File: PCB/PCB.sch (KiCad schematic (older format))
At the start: 40 parts, among them J1 Dynamo, J10 Conn_01x08_Female, J11 Conn_01x01_Female, J12 Conn_01x04_Female, J2 Conn_01x28_Female, J3 Conn_01x02_Female, J4 Conn_01x02_Female, J5 Conn_01x02_Female, J6 Conn_01x02_Female, J7 Conn_01x08_Female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

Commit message: Added PCB images
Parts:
- removed J1: Dynamo, TerminalBlock:TerminalBlock_Altech_AK300-2_P5.00mm, symbol Connector:Screw_Terminal_01x02
- added J1: Conn_01x04_Female, Connector_Molex:Molex_KK-396_A-41791-0004_1x04_P3.96mm_Vertical, symbol Connector:Conn_01x04_Female
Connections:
- net at D2.1 (K), D4.2 (A): now also J1.1 (Pin_1), J1.2 (Pin_2)
- net at D1.1 (K), D3.2 (A): now also J1.3 (Pin_3), J1.4 (Pin_4)
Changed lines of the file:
@@
 EESchema Schematic File Version 4
 LIBS:PCB-cache
-EELAYER 29 0
+EELAYER 26 0
 EELAYER END
 $Descr A4 11693 8268
@@
 	-1   0    0    1
 $EndComp
-$Comp
-L Connector:Screw_Terminal_01x02 J1
-U 1 1 5E63414E
-P 1550 1300
-F 0 "J1" H 1550 950 50  0000 C CNN
-F 1 "Dynamo" H 1550 1050 50  0000 C CNN
-F 2 "TerminalBlock:TerminalBlock_Altech_AK300-2_P5.00mm" H 1550 1300 50  0001 C CNN
-F 3 "~" H 1550 1300 50  0001 C CNN
-	1    1550 1300
-	-1   0    0    1
-$EndComp
 Wire Wire Line
 	2100 1050 2000 1050
@@
 NoConn ~ 2850 4450
 NoConn ~ 2850 4550
+$Comp
+L Connector:Conn_01x04_Female J1
+U 1 1 5E2F9CB0
+P 1450 1300
+F 0 "J1" H 1344 875 50  0000 C CNN
+F 1 "Conn_01x04_Female" H 1344 966 50  0000 C CNN
+F 2 "Connector_Molex:Molex_KK-396_A-41791-0004_1x04_P3.96mm_Vertical" H 1450 1300 50  0001 C CNN
+F 3 "~" H 1450 1300 50  0001 C CNN
+	1    1450 1300
+	-1   0    0    1
+$EndComp
+Wire Wire Line
+	1750 1200 1650 1200
+Wire Wire Line
+	1750 1300 1650 1300
+Wire Wire Line
+	1650 1200 1650 1100
+Connection ~ 1650 1200
+Wire Wire Line
+	1650 1300 1650 1400
+Connection ~ 1650 1300
 $EndSCHEMATC

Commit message: Added GPS control logic
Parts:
- added Q1: PN2222A, Package_TO_SOT_THT:TO-92_Inline, symbol Transistor_BJT:PN2222A
- added Q2: IRF4905, Package_TO_SOT_THT:TO-220-3_Vertical, symbol Transistor_FET:IRF4905
- added R3: 1k, Resistor_THT:R_Axial_DIN0207_L6.3mm_D2.5mm_P10.16mm_Horizontal, symbol Device:R
- added R4: 4.7k, Resistor_THT:R_Axial_DIN0207_L6.3mm_D2.5mm_P10.16mm_Horizontal, symbol Device:R
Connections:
- net +5V: now also Q2.3 (S), R4.2; no longer J12.1 (Pin_1)
- net GND: now also Q1.1 (E)
- net GPSEN: now reaches J2.28 (Pin_28)
- net GPSEN: now also R3.1
- new net: Q1.2 (B), R3.2
- new net: Q1.3 (C), Q2.1 (G), R4.1
- new net VCCGPS: J12.1 (Pin_1), Q2.2 (D)
- no-connect marks 14 -> 13
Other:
- moved on the sheet: C15, J12, J8, R2
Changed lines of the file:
@@
 $EndComp
 Wire Wire Line
-	9650 5300 9500 5300
-Wire Wire Line
-	9650 5400 9500 5400
-Text GLabel 9500 5400 0    50   Input ~ 0
+	9100 4200 8950 4200
+Wire Wire Line
+	9100 4300 8950 4300
+Text GLabel 8950 4300 0    50   Input ~ 0
 RX
 Wire Wire Line
@@
 Text GLabel 2650 5650 0    50   Input ~ 0
 RX
-Text GLabel 9500 5300 0    50   Input ~ 0
+Text GLabel 8950 4200 0    50   Input ~ 0
 TX
 Wire Wire Line
@@
 TX
 Wire Wire Line
-	9650 5500 9500 5500
-Wire Wire Line
-	9650 5200 9500 5200
-Wire Wire Line
-	9500 5200 9500 5150
-$Comp
-L power:+5V #PWR026
-U 1 1 5E2D514F
-P 9500 5150
-F 0 "#PWR026" H 9500 5000 50  0001 C CNN
-F 1 "+5V" H 9515 5323 50  0000 C CNN
-F 2 "" H 9500 5150 50  0001 C CNN
-F 3 "" H 9500 5150 50  0001 C CNN
-	1    9500 5150
-	1    0    0    -1
-$EndComp
-Wire Wire Line
-	9500 5500 9500 5550
+	9100 4400 8950 4400
+Wire Wire Line
+	9100 4100 8950 4100
+Wire Wire Line
+	8950 4400 8950 4450
 $Comp
 L power:GND #PWR027
 U 1 1 5E2D7839
-P 9500 5550
-F 0 "#PWR027" H 9500 5300 50  0001 C CNN
-F 1 "GND" H 9505 5377 50  0000 C CNN
-F 2 "" H 9500 5550 50  0001 C CNN
-F 3 "" H 9500 5550 50  0001 C CNN
-	1    9500 5550
+P 8950 4450
+F 0 "#PWR027" H 8950 4200 50  0001 C CNN
+F 1 "GND" H 8955 4277 50  0000 C CNN
+F 2 "" H 8950 4450 50  0001 C CNN
+F 3 "" H 8950 4450 50  0001 C CNN
+	1    8950 4450
 	1    0    0    -1
 $EndComp
@@
 	6450 1650 6850 1650
 Wire Wire Line
-	8650 5350 8650 5650
+	7900 4250 7900 4550
 $Comp
 L power:GND #PWR021
 U 1 1 5E671D81
-P 8650 5650
-F 0 "#PWR021" H 8650 5400 50  0001 C CNN
-F 1 "GND" H 8655 5477 50  0000 C CNN
-F 2 "" H 8650 5650 50  0001 C CNN
-F 3 "" H 8650 5650 50  0001 C CNN
-	1    8650 5650
+P 7900 4550
+F 0 "#PWR021" H 7900 4300 50  0001 C CNN
+F 1 "GND" H 7905 4377 50  0000 C CNN
+F 2 "" H 7900 4550 50  0001 C CNN
+F 3 "" H 7900 4550 50  0001 C CNN
+	1    7900 4550
 	1    0    0    -1
 $EndComp
@@
 L Connector:Conn_01x04_Female J12
 U 1 1 5E3CD64F
-P 9850 5300
-F 0 "J12" H 9878 5276 50  0000 L CNN
-F 1 "Conn_01x04_Female" H 9878 5185 50  0000 L CNN
-F 2 "Connector_PinSocket_2.54mm:PinSocket_1x04_P2.54mm_Vertical" H 9850 5300 50  0001 C CNN
-F 3 "~" H 9850 5300 50  0001 C CNN
-	1    9850 5300
+P 9300 4200
+F 0 "J12" H 9328 4176 50  0000 L CNN
+F 1 "Conn_01x04_Female" H 9328 4085 50  0000 L CNN
+F 2 "Connector_PinSocket_2.54mm:PinSocket_1x04_P2.54mm_Vertical" H 9300 4200 50  0001 C CNN
+F 3 "~" H 9300 4200 50  0001 C CNN
+	1    9300 4200
 	1    0    0    -1
 $EndComp
@@
 L Connector:Conn_01x02_Female J8
 U 1 1 5E3EA4DC
-P 8300 5150
-F 0 "J8" V 8238 4962 50  0000 R CNN
-F 1 "Conn_01x02_Female" V 8147 4962 50  0000 R CNN
-F 2 "Connector_Molex:Molex_PicoBlade_53047-0210_1x02_P1.25mm_Vertical" H 8300 5150 50  0001 C CNN
-F 3 "~" H 8300 5150 50  0001 C CNN
-	1    8300 5150
+P 7550 4050
+F 0 "J8" V 7488 3862 50  0000 R CNN
+F 1 "Conn_01x02_Female" V 7397 3862 50  0000 R CNN
+F 2 "Connector_Molex:Molex_PicoBlade_53047-0210_1x02_P1.25mm_Vertical" H 7550 4050 50  0001 C CNN
+F 3 "~" H 7550 4050 50  0001 C CNN
+	1    7550 4050
 	0    -1   -1   0
 $EndComp
 Wire Wire Line
-	8400 5350 8650 5350
+	7650 4250 7900 4250
 $Comp
 L Connector:Conn_01x08_Female J7
@@
 NSS
 $Comp
-L Connector:Conn_01x28_Female J2
-U 1 1 5E7FA35C
-P 3050 5650
-F 0 "J2" H 3078 5626 50  0000 L CNN
-F 1 "Conn_01x28_Female" H 3078 5535 50  0000 L CNN
-F 2 "Package_DIP:DIP-28_W7.62mm" H 3050 5650 50  0001 C CNN
-F 3 "~" H 3050 5650 50  0001 C CNN
-	1    3050 5650
-	1    0    0    -1
-$EndComp
-$Comp
 L Device:C_Small C5
 U 1 1 5E7AF997
@@
 NoConn ~ 2850 6850
 NoConn ~ 2850 6950
-NoConn ~ 2850 7050
 $Comp
 L Connector:Conn_01x02_Female J3
@@
 	8500 1250 8900 1250
 NoConn ~ 2850 6650
-Text GLabel 7600 5350 0    50   Input ~ 0
+Text GLabel 6850 4250 0    50   Input ~ 0
 BUTTON
 $Comp
 L Device:R R2
 U 1 1 5ECC6F67
-P 7900 5350
-F 0 "R2" V 8050 5350 50  0000 L CNN
-F 1 "1k" V 7970 5305 50  0000 L CNN
-F 2 "Resistor_THT:R_Axial_DIN0207_L6.3mm_D2.5mm_P10.16mm_Horizontal" V 7830 5350 50  0001 C CNN
-F 3 "~" H 7900 5350 50  0001 C CNN
-	1    7900 5350
+P 7150 4250
+F 0 "R2" V 7300 4250 50  0000 L CNN
+F 1 "1k" V 7220 4205 50  0000 L CNN
+F 2 "Resistor_THT:R_Axial_DIN0207_L6.3mm_D2.5mm_P10.16mm_Horizontal" V 7080 4250 50  0001 C CNN
+F 3 "~" H 7150 4250 50  0001 C CNN
+	1    7150 4250
 	0    -1   -1   0
 $EndComp
 Wire Wire Line
-	7600 5350 7750 5350
-Wire Wire Line
-	8200 5350 8300 5350
-Connection ~ 8200 5350
-Wire Wire Line
-	8050 5350 8200 5350
+	6850 4250 7000 4250
+Wire Wire Line
+	7450 4250 7550 4250
+Connection ~ 7450 4250
+Wire Wire Line
+	7300 4250 7450 4250
 $Comp
 L power:GND #PWR018
 U 1 1 5ECB146B
-P 8200 5650
-F 0 "#PWR018" H 8200 5400 50  0001 C CNN
-F 1 "GND" H 8205 5477 50  0000 C CNN
-F 2 "" H 8200 5650 50  0001 C CNN
-F 3 "" H 8200 5650 50  0001 C CNN
-	1    8200 5650
-	1    0    0    -1
-$EndComp
-Wire Wire Line
-	8200 5350 8200 5400
-Wire Wire Line
-	8200 5600 8200 5650
+P 7450 4550
+F 0 "#PWR018" H 7450 4300 50  0001 C CNN
+F 1 "GND" H 7455 4377 50  0000 C CNN
+F 2 "" H 7450 4550 50  0001 C CNN
+F 3 "" H 7450 4550 50  0001 C CNN
+	1    7450 4550
+	1    0    0    -1
+$EndComp
+Wire Wire Line
+	7450 4250 7450 4300
+Wire Wire Line
+	7450 4500 7450 4550
 $Comp
 L Device:C_Small C15
 U 1 1 5EC75BB7
-P 8200 5500
-F 0 "C15" H 8292 5546 50  0000 L CNN
-F 1 "100n" H 8292 5455 50  0000 L CNN
-F 2 "Capacitor_THT:C_Disc_D3.0mm_W2.0mm_P2.50mm" H 8200 5500 50  0001 C CNN
-F 3 "~" H 8200 5500 50  0001 C CNN
-	1    8200 5500
+P 7450 4400
+F 0 "C15" H 7542 4446 50  0000 L CNN
+F 1 "100n" H 7542 4355 50  0000 L CNN
+F 2 "Capacitor_THT:C_Disc_D3.0mm_W2.0mm_P2.50mm" H 7450 4400 50  0001 C CNN
+F 3 "~" H 7450 4400 50  0001 C CNN
+	1    7450 4400
 	1    0    0    -1
 $EndComp
@@
 	1650 1300 1650 1400
 Connection ~ 1650 1300
+$Comp
+L Device:R R3
+U 1 1 5E30BB98
+P 7250 5850
+F 0 "R3" V 7457 5850 50  0000 C CNN
+F 1 "1k" V 7366 5850 50  0000 C CNN
+F 2 "Resistor_THT:R_Axial_DIN0207_L6.3mm_D2.5mm_P10.16mm_Horizontal" V 7180 5850 50  0001 C CNN
+F 3 "~" H 7250 5850 50  0001 C CNN
+	1    7250 5850
+	0    -1   -1   0
+$EndComp
+$Comp
+L Device:R R4
+U 1 1 5E31ACDB
+P 7400 5400
+F 0 "R4" H 7330 5354 50  0000 R CNN
+F 1 "4.7k" H 7330 5445 50  0000 R CNN
+F 2 "Resistor_THT:R_Axial_DIN0207_L6.3mm_D2.5mm_P10.16mm_Horizontal" V 7330 5400 50  0001 C CNN
+F 3 "~" H 7400 5400 50  0001 C CNN
+	1    7400 5400
+	-1   0    0    1
+$EndComp
+$Comp
+L Transistor_BJT:PN2222A Q1
+U 1 1 5E338DF7
+P 7750 5850
+F 0 "Q1" H 7941 5896 50  0000 L CNN
+F 1 "PN2222A" H 7941 5805 50  0000 L CNN
+F 2 "Package_TO_SOT_THT:TO-92_Inline" H 7950 5775 50  0001 L CIN
+F 3 "http://www.fairchildsemi.com/ds/PN/PN2222A.pdf" H 7750 5850 50  0001 L CNN
+	1    7750 5850
+	1    0    0    -1
+$EndComp
+$Comp
+L Transistor_FET:IRF4905 Q2
+U 1 1 5E338EAB
+P 7850 5300
+F 0 "Q2" V 8193 5300 50  0000 C CNN
+F 1 "IRF4905" V 8102 5300 50  0000 C CNN
+F 2 "Package_TO_SOT_THT:TO-220-3_Vertical" H 8050 5225 50  0001 L CIN
+F 3 "http://www.infineon.com/dgdl/irf4905.pdf?fileId=5546d462533600a4015355e32165197c" H 7850 5300 50  0001 L CNN
+	1    7850 5300
+	0    1    -1   0
+$EndComp
+$Comp
+L Connector:Conn_01x28_Female J2
+U 1 1 5E7FA35C
+P 3050 5650
+F 0 "J2" H 3078 5626 50  0000 L CNN
+F 1 "Conn_01x28_Female" H 3078 5535 50  0000 L CNN
+F 2 "Package_DIP:DIP-28_W7.62mm" H 3050 5650 50  0001 C CNN
+F 3 "~" H 3050 5650 50  0001 C CNN
+	1    3050 5650
+	1    0    0    -1
+$EndComp
+Wire Wire Line
+	2850 7050 2650 7050
+Text GLabel 2650 7050 0    50   Input ~ 0
+GPSEN
+Wire Wire Line
+	7100 5850 6900 5850
+Text GLabel 6900 5850 0    50   Input ~ 0
+GPSEN
+Wire Wire Line
+	7400 5850 7550 5850
+Wire Wire Line
+	7850 6050 7850 6150
+$Comp
+L power:GND #PWR028
+U 1 1 5E397848
+P 7850 6150
+F 0 "#PWR028" H 7850 5900 50  0001 C CNN
+F 1 "GND" H 7855 5977 50  0000 C CNN
+F 2 "" H 7850 6150 50  0001 C CNN
+F 3 "" H 7850 6150 50  0001 C CNN
+	1    7850 6150
+	1    0    0    -1
+$EndComp
+Wire Wire Line
+	7850 5650 7850 5600
+Wire Wire Line
+	7850 5600 7400 5600
+Wire Wire Line
+	7400 5600 7400 5550
+Connection ~ 7850 5600
+Wire Wire Line
+	7850 5600 7850 5500
+Wire Wire Line
+	7400 5250 7400 5200
+Wire Wire Line
+	7400 5200 7650 5200
+Wire Wire Line
+	7400 5200 7400 5150
+Connection ~ 7400 5200
+$Comp
+L power:+5V #PWR026
+U 1 1 5E3C04A1
+P 7400 5150
+F 0 "#PWR026" H 7400 5000 50  0001 C CNN
+F 1 "+5V" H 7415 5323 50  0000 C CNN
+F 2 "" H 7400 5150 50  0001 C CNN
+F 3 "" H 7400 5150 50  0001 C CNN
+	1    7400 5150
+	1    0    0    -1
+$EndComp
+Wire Wire Line
+	8050 5200 8250 5200
+Text GLabel 8250 5200 2    50   Input ~ 0
+VCCGPS
+Text GLabel 8950 4100 0    50   Input ~ 0
+VCCGPS
 $EndSCHEMATC

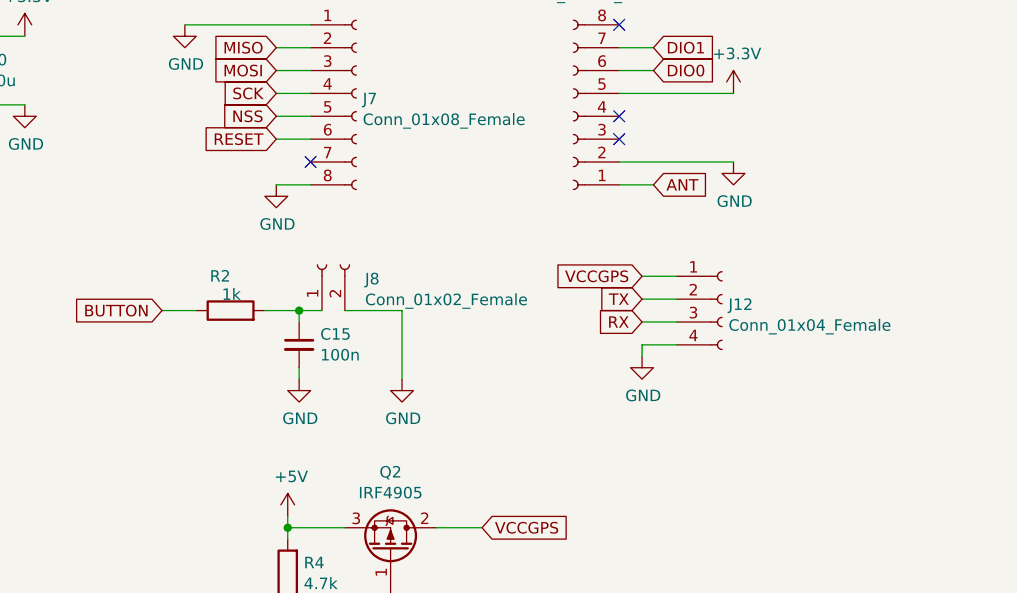
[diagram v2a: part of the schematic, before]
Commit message: fixed PCB layout and transmitter data fetch bug
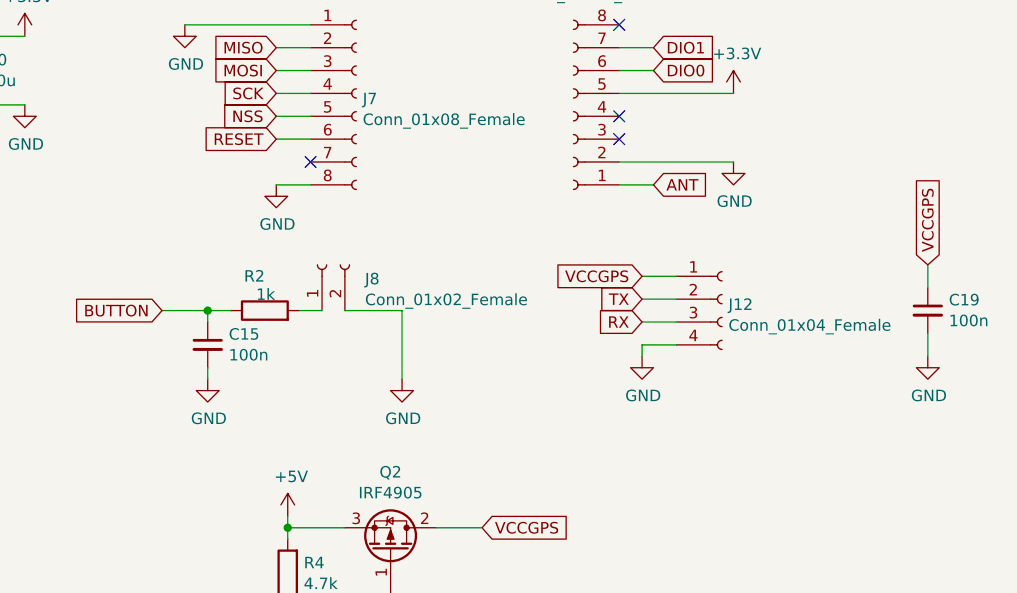
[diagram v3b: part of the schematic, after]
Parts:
- added C19: 100n, Capacitor_THT:C_Disc_D3.0mm_W2.0mm_P2.50mm, symbol Device:C_Small
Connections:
- net BUTTON: now also C15.1
- net GND: now also C19.2
- net VCCGPS: now also C19.1
- net at J8.1 (Pin_1), R2.2: no longer C15.1
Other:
- moved on the sheet: C15, R2
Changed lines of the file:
@@
 L Device:R R2
 U 1 1 5ECC6F67
-P 7150 4250
-F 0 "R2" V 7300 4250 50  0000 L CNN
-F 1 "1k" V 7220 4205 50  0000 L CNN
-F 2 "Resistor_THT:R_Axial_DIN0207_L6.3mm_D2.5mm_P10.16mm_Horizontal" V 7080 4250 50  0001 C CNN
-F 3 "~" H 7150 4250 50  0001 C CNN
-	1    7150 4250
+P 7300 4250
+F 0 "R2" V 7450 4250 50  0000 L CNN
+F 1 "1k" V 7370 4205 50  0000 L CNN
+F 2 "Resistor_THT:R_Axial_DIN0207_L6.3mm_D2.5mm_P10.16mm_Horizontal" V 7230 4250 50  0001 C CNN
+F 3 "~" H 7300 4250 50  0001 C CNN
+	1    7300 4250
 	0    -1   -1   0
 $EndComp
-Wire Wire Line
-	6850 4250 7000 4250
-Wire Wire Line
-	7450 4250 7550 4250
-Connection ~ 7450 4250
-Wire Wire Line
-	7300 4250 7450 4250
 $Comp
 L power:GND #PWR018
 U 1 1 5ECB146B
-P 7450 4550
-F 0 "#PWR018" H 7450 4300 50  0001 C CNN
-F 1 "GND" H 7455 4377 50  0000 C CNN
-F 2 "" H 7450 4550 50  0001 C CNN
-F 3 "" H 7450 4550 50  0001 C CNN
-	1    7450 4550
-	1    0    0    -1
-$EndComp
-Wire Wire Line
-	7450 4250 7450 4300
-Wire Wire Line
-	7450 4500 7450 4550
+P 7050 4550
+F 0 "#PWR018" H 7050 4300 50  0001 C CNN
+F 1 "GND" H 7055 4377 50  0000 C CNN
+F 2 "" H 7050 4550 50  0001 C CNN
+F 3 "" H 7050 4550 50  0001 C CNN
+	1    7050 4550
+	1    0    0    -1
+$EndComp
+Wire Wire Line
+	7050 4250 7050 4300
+Wire Wire Line
+	7050 4500 7050 4550
 $Comp
 L Device:C_Small C15
 U 1 1 5EC75BB7
-P 7450 4400
-F 0 "C15" H 7542 4446 50  0000 L CNN
-F 1 "100n" H 7542 4355 50  0000 L CNN
-F 2 "Capacitor_THT:C_Disc_D3.0mm_W2.0mm_P2.50mm" H 7450 4400 50  0001 C CNN
-F 3 "~" H 7450 4400 50  0001 C CNN
-	1    7450 4400
+P 7050 4400
+F 0 "C15" H 7142 4446 50  0000 L CNN
+F 1 "100n" H 7142 4355 50  0000 L CNN
+F 2 "Capacitor_THT:C_Disc_D3.0mm_W2.0mm_P2.50mm" H 7050 4400 50  0001 C CNN
+F 3 "~" H 7050 4400 50  0001 C CNN
+	1    7050 4400
 	1    0    0    -1
 $EndComp
@@
 Text GLabel 8950 4100 0    50   Input ~ 0
 VCCGPS
+Wire Wire Line
+	7450 4250 7550 4250
+Connection ~ 7050 4250
+Wire Wire Line
+	7050 4250 7150 4250
+Wire Wire Line
+	6850 4250 7050 4250
+$Comp
+L Device:C_Small C19
+U 1 1 5E40C6E0
+P 10200 4250
+F 0 "C19" H 10292 4296 50  0000 L CNN
+F 1 "100n" H 10292 4205 50  0000 L CNN
+F 2 "Capacitor_THT:C_Disc_D3.0mm_W2.0mm_P2.50mm" H 10200 4250 50  0001 C CNN
+F 3 "~" H 10200 4250 50  0001 C CNN
+	1    10200 4250
+	1    0    0    -1
+$EndComp
+Wire Wire Line
+	10200 4150 10200 4050
+Text GLabel 10200 4050 1    50   Input ~ 0
+VCCGPS
+$Comp
+L power:GND #PWR029
+U 1 1 5E436C44
+P 10200 4450
+F 0 "#PWR029" H 10200 4200 50  0001 C CNN
+F 1 "GND" H 10205 4277 50  0000 C CNN
+F 2 "" H 10200 4450 50  0001 C CNN
+F 3 "" H 10200 4450 50  0001 C CNN
+	1    10200 4450
+	1    0    0    -1
+$EndComp
+Wire Wire Line
+	10200 4350 10200 4450
 $EndSCHEMATC

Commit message: Finished Transmitter code and PCB
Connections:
- net BUTTON: now also J2.5 (Pin_5); no longer J2.23 (Pin_23)
- net DIO1: no longer J2.5 (Pin_5)
- net at J1.1 (Pin_1), J1.2 (Pin_2): now also D1.1 (K), D3.2 (A); no longer D2.1 (K), D4.2 (A)
- net at J1.3 (Pin_3), J1.4 (Pin_4): now also D2.1 (K), D4.2 (A); no longer D1.1 (K), D3.2 (A)
- no-connect marks 13 -> 14
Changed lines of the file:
@@
 DIO0
-Wire Wire Line
-	2850 4750 2650 4750
-Text GLabel 2650 4750 0    50   Input ~ 0
-DIO1
 Wire Wire Line
 	1500 4100 1700 4100
@@
 NoConn ~ 2850 5450
 NoConn ~ 2850 5550
-Text GLabel 2650 6550 0    50   Input ~ 0
-BUTTON
-Wire Wire Line
-	2850 6550 2650 6550
 Wire Wire Line
 	2850 6450 2250 6450
@@
 L Connector:Conn_01x04_Female J1
 U 1 1 5E2F9CB0
-P 1450 1300
-F 0 "J1" H 1344 875 50  0000 C CNN
-F 1 "Conn_01x04_Female" H 1344 966 50  0000 C CNN
-F 2 "Connector_Molex:Molex_KK-396_A-41791-0004_1x04_P3.96mm_Vertical" H 1450 1300 50  0001 C CNN
-F 3 "~" H 1450 1300 50  0001 C CNN
-	1    1450 1300
-	-1   0    0    1
+P 1450 1200
+F 0 "J1" H 1344 775 50  0000 C CNN
+F 1 "Conn_01x04_Female" H 1344 866 50  0000 C CNN
+F 2 "Connector_Molex:Molex_KK-396_A-41791-0004_1x04_P3.96mm_Vertical" H 1450 1200 50  0001 C CNN
+F 3 "~" H 1450 1200 50  0001 C CNN
+	1    1450 1200
+	-1   0    0    -1
 $EndComp
 Wire Wire Line
@@
 Wire Wire Line
 	1650 1200 1650 1100
-Connection ~ 1650 1200
 Wire Wire Line
 	1650 1300 1650 1400
-Connection ~ 1650 1300
 $Comp
 L Device:R R3
@@
 Wire Wire Line
 	10200 4350 10200 4450
+NoConn ~ 2850 6550
+Text GLabel 2650 4750 0    50   Input ~ 0
+BUTTON
+Wire Wire Line
+	2850 4750 2650 4750
+Connection ~ 1650 1200
+Connection ~ 1650 1300
 $EndSCHEMATC

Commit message: Updated Schematic and PCB
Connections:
- net DIO1: no longer names the net of J10.7 (Pin_7)
- no-connect marks 14 -> 15
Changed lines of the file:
@@
 NoConn ~ 8850 3400
 Wire Wire Line
-	9000 3100 8850 3100
-Wire Wire Line
 	9000 3200 8850 3200
 Wire Wire Line
 	9000 3700 8850 3700
-Text GLabel 9000 3100 2    50   Input ~ 0
-DIO1
 Text GLabel 9000 3200 2    50   Input ~ 0
 DIO0
@@
 Connection ~ 1650 1200
 Connection ~ 1650 1300
+NoConn ~ 8850 3100
 $EndSCHEMATC

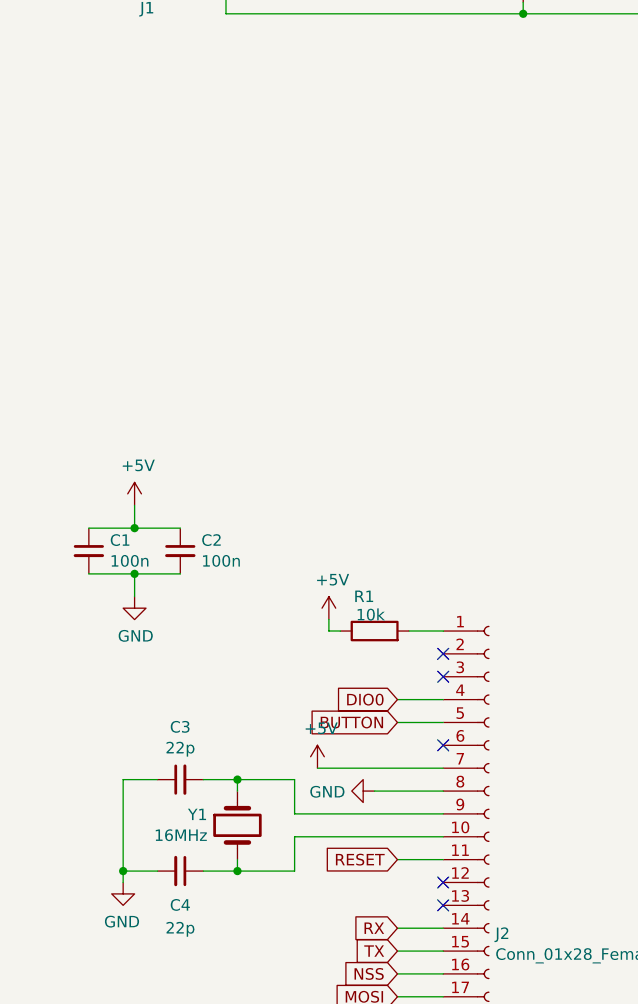
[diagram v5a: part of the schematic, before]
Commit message: Added UART Header
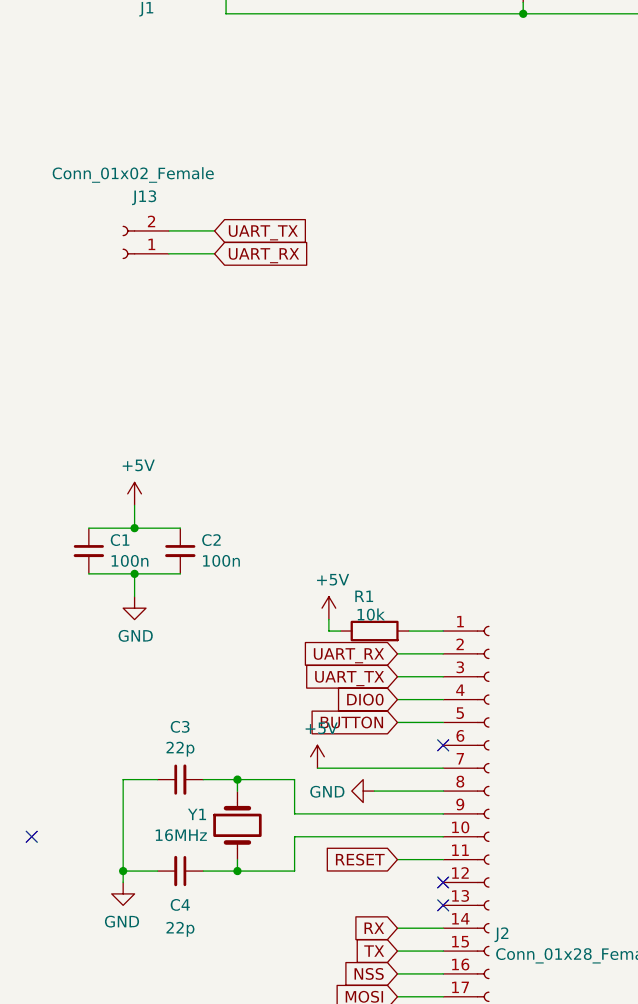
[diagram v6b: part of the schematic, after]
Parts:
- added J13: Conn_01x02_Female, Connector_PinSocket_2.54mm:PinSocket_1x02_P2.54mm_Vertical, symbol Connector:Conn_01x02_Female
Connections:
- net UART_RX: now reaches J2.2 (Pin_2)
- net UART_RX: now also J13.1 (Pin_1)
- net UART_TX: now reaches J2.3 (Pin_3)
- net UART_TX: now also J13.2 (Pin_2)
- no-connect marks 15 -> 14
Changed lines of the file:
@@
 	1    0    0    -1
 $EndComp
-NoConn ~ 2850 4450
-NoConn ~ 2850 4550
 $Comp
 L Connector:Conn_01x04_Female J1
@@
 Connection ~ 1650 1300
 NoConn ~ 8850 3100
+NoConn ~ 1050 5250
+$Comp
+L Connector:Conn_01x02_Female J13
+U 1 1 5E38F499
+P 1450 2700
+F 0 "J13" H 1300 2450 50  0000 L CNN
+F 1 "Conn_01x02_Female" H 1050 2350 50  0000 L CNN
+F 2 "Connector_PinSocket_2.54mm:PinSocket_1x02_P2.54mm_Vertical" H 1450 2700 50  0001 C CNN
+F 3 "~" H 1450 2700 50  0001 C CNN
+	1    1450 2700
+	-1   0    0    1
+$EndComp
+Text GLabel 2650 4450 0    50   Input ~ 0
+UART_RX
+Wire Wire Line
+	2850 4450 2650 4450
+Text GLabel 2650 4550 0    50   Input ~ 0
+UART_TX
+Wire Wire Line
+	2850 4550 2650 4550
+Text GLabel 1850 2700 2    50   Input ~ 0
+UART_RX
+Wire Wire Line
+	1650 2700 1850 2700
+Text GLabel 1850 2600 2    50   Input ~ 0
+UART_TX
+Wire Wire Line
+	1650 2600 1850 2600
 $EndSCHEMATC
